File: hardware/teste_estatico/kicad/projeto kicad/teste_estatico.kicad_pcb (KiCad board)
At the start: 2 copper layers, 10 parts, among them J1 PINHD_1x6_Female

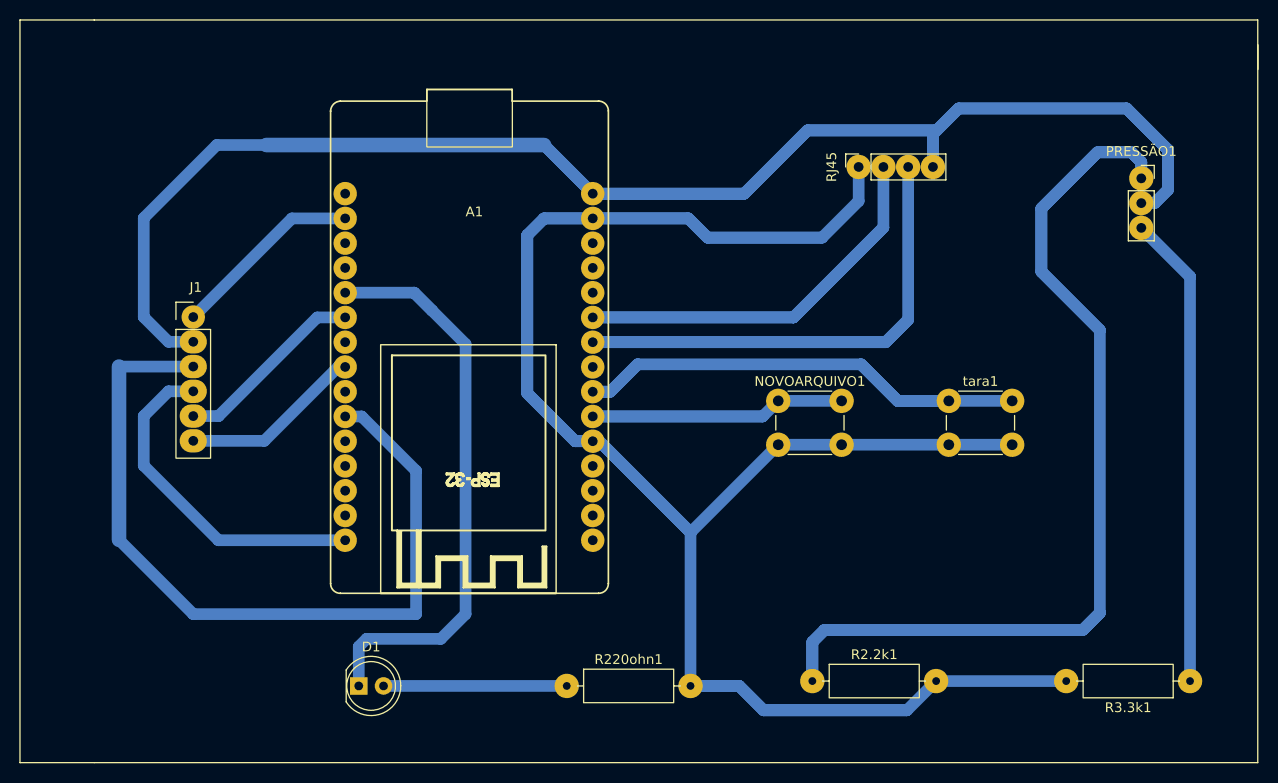
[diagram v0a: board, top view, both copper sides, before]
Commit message: feat: adcionado arquivos de fabricação e modificação na pcb
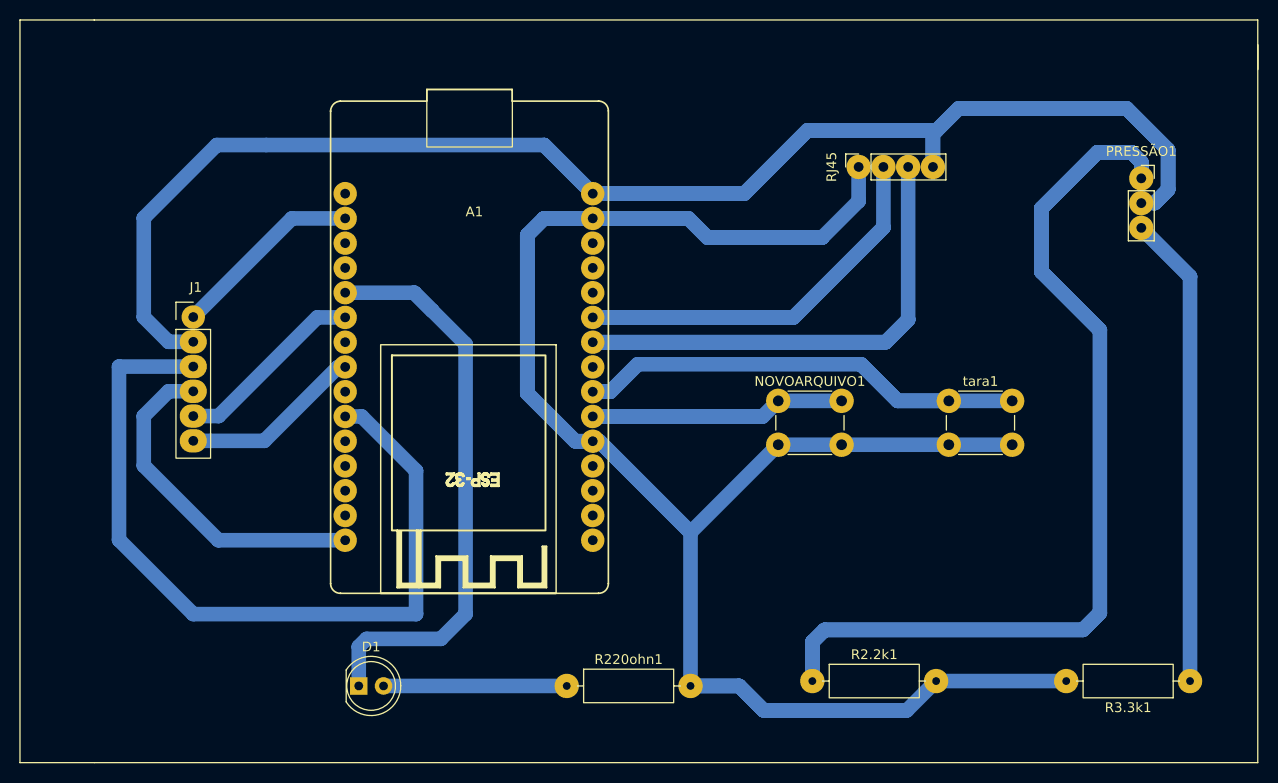
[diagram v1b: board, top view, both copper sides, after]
